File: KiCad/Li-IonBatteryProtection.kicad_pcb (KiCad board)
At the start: 2 copper layers, 1 part, among them Q1 IRF540N

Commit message: Net wiring on PCB is done.
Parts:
- added C1: 0.1uf, Capacitors_ThroughHole:C_Rect_L4_W2.5_P2.5, F.Cu at (184.2, 119.4)
- added C2: 0.22uf, Capacitors_ThroughHole:C_Rect_L7_W2_P5, F.Cu at (190.5, 116.8)
- added C3: 0.001uf, Capacitors_ThroughHole:C_Rect_L7_W2_P5, F.Cu at (188.0, 101.6)
- added C4: 47uf, Capacitors_ThroughHole:C_Radial_D5_L11_P2.5, F.Cu at (203.2, 105.4)
- added D1: 1N4728, Diodes_ThroughHole:Diode_DO-41_SOD81_Horizontal_RM10, F.Cu at (67.3, 113.0)
- added D2: 1N4728, Diodes_ThroughHole:Diode_DO-41_SOD81_Horizontal_RM10, F.Cu at (99.1, 113.0)
- added D3: 1N4728, Diodes_ThroughHole:Diode_DO-41_SOD81_Horizontal_RM10, F.Cu at (130.8, 113.0)
- added D4: 1N4728, Diodes_ThroughHole:Diode_DO-41_SOD81_Horizontal_RM10, F.Cu at (162.6, 113.0)
- added J1: CONN_02X03, Pin_Headers:Pin_Header_Straight_2x03, F.Cu at (218.4, 82.5)
- added J2: CONN_01X02, Terminal_Blocks:TerminalBlock_Pheonix_MKDS1.5-2pol, F.Cu at (209.6, 82.5)
- added Q2: 2N2222A, TO_SOT_Packages_THT:TO-18_3Pin, F.Cu at (201.9, 119.4)
- added Q3: 2N2222A, TO_SOT_Packages_THT:TO-18_3Pin, F.Cu at (81.3, 90.2)
- added Q4: 2N2222A, TO_SOT_Packages_THT:TO-18_3Pin, F.Cu at (113.0, 90.2)
- added Q5: 2N2222A, TO_SOT_Packages_THT:TO-18_3Pin, F.Cu at (144.8, 90.2)
- added Q6: 2N2222A, TO_SOT_Packages_THT:TO-18_3Pin, F.Cu at (176.5, 90.2)
- added R1: 10k, Resistors_ThroughHole:Resistor_Horizontal_RM10mm, F.Cu at (67.3, 105.4)
- added R10: 1Meg, Potentiometers:Potentiometer_Bourns_3296Y_3-8Zoll_Angular_ScrewUp, F.Cu at (96.5, 119.4)
- added R11: 47k, Resistors_ThroughHole:Resistor_Horizontal_RM10mm, F.Cu at (105.4, 92.7)
- added R12: 100k, Resistors_ThroughHole:Resistor_Horizontal_RM10mm, F.Cu at (88.9, 90.2)
- added R13: 100, Resistors_ThroughHole:Resistor_Horizontal_RM10mm, F.Cu at (113.0, 96.5)
- added R14: 120, Resistors_ThroughHole:Resistor_Horizontal_RM10mm, F.Cu at (88.9, 82.5)
- added R15: 10k, Resistors_ThroughHole:Resistor_Horizontal_RM10mm, F.Cu at (130.8, 105.4)
- added R16: 1k, Resistors_ThroughHole:Resistor_Horizontal_RM7mm, F.Cu at (120.7, 97.8)
- added R17: 1Meg, Potentiometers:Potentiometer_Bourns_3296Y_3-8Zoll_Angular_ScrewUp, F.Cu at (128.3, 119.4)
- added R18: 47k, Resistors_ThroughHole:Resistor_Horizontal_RM10mm, F.Cu at (137.2, 92.7)
- added R19: 100k, Resistors_ThroughHole:Resistor_Horizontal_RM10mm, F.Cu at (120.7, 90.2)
- added R2: 1k, Resistors_ThroughHole:Resistor_Horizontal_RM7mm, F.Cu at (57.1, 97.8)
- added R20: 100, Resistors_ThroughHole:Resistor_Horizontal_RM10mm, F.Cu at (144.8, 96.5)
- added R21: 120, Resistors_ThroughHole:Resistor_Horizontal_RM10mm, F.Cu at (120.7, 82.5)
- added R22: 10k, Resistors_ThroughHole:Resistor_Horizontal_RM10mm, F.Cu at (162.6, 105.4)
- added R23: 1k, Resistors_ThroughHole:Resistor_Horizontal_RM7mm, F.Cu at (152.4, 97.8)
- added R24: 1Meg, Potentiometers:Potentiometer_Bourns_3296Y_3-8Zoll_Angular_ScrewUp, F.Cu at (160.0, 119.4)
- added R25: 47k, Resistors_ThroughHole:Resistor_Horizontal_RM10mm, F.Cu at (168.9, 92.7)
- added R26: 100k, Resistors_ThroughHole:Resistor_Horizontal_RM10mm, F.Cu at (152.4, 90.2)
- added R27: 100, Resistors_ThroughHole:Resistor_Horizontal_RM10mm, F.Cu at (176.5, 96.5)
- added R28: 120, Resistors_ThroughHole:Resistor_Horizontal_RM10mm, F.Cu at (152.4, 82.5)
- added R29: 5.1k, Resistors_ThroughHole:Resistor_Horizontal_RM10mm, F.Cu at (194.3, 110.5)
- added R3: 1Meg, Potentiometers:Potentiometer_Bourns_3296Y_3-8Zoll_Angular_ScrewUp, F.Cu at (64.8, 119.4)
- added R30: 3.3k, Resistors_ThroughHole:Resistor_Horizontal_RM10mm, F.Cu at (196.8, 88.9)
- added R31: 20k, Resistors_ThroughHole:Resistor_Horizontal_RM10mm, F.Cu at (194.3, 80.0)
- added R4: 47k, Resistors_ThroughHole:Resistor_Horizontal_RM10mm, F.Cu at (73.7, 94.0)
- added R5: 100k, Resistors_ThroughHole:Resistor_Horizontal_RM10mm, F.Cu at (57.1, 90.2)
- added R6: 100, Resistors_ThroughHole:Resistor_Horizontal_RM10mm, F.Cu at (81.3, 96.5)
- added R7: 120, Resistors_ThroughHole:Resistor_Horizontal_RM10mm, F.Cu at (57.1, 82.5)
- added R8: 10k, Resistors_ThroughHole:Resistor_Horizontal_RM10mm, F.Cu at (99.1, 105.4)
- added R9: 1k, Resistors_ThroughHole:Resistor_Horizontal_RM7mm, F.Cu at (88.9, 97.8)
- added U1: LM311N, Housings_DIP:DIP-8_W7.62mm, F.Cu at (74.9, 113.0)
- added U2: PC817, Housings_DIP:DIP-4_W7.62mm, F.Cu at (74.9, 80.0)
- added U3: LM311N, Housings_DIP:DIP-8_W7.62mm, F.Cu at (106.7, 113.0)
- added U4: PC817, Housings_DIP:DIP-4_W7.62mm, F.Cu at (106.7, 80.0)
- added U5: LM311N, Housings_DIP:DIP-8_W7.62mm, F.Cu at (138.4, 113.0)
- added U6: PC817, Housings_DIP:DIP-4_W7.62mm, F.Cu at (138.4, 80.0)
- added U7: LM311N, Housings_DIP:DIP-8_W7.62mm, F.Cu at (170.2, 113.0)
- added U8: PC817, Housings_DIP:DIP-4_W7.62mm, F.Cu at (170.2, 80.0)
- moved Q1 80.7 mm to (219.7, 118.1)
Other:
- board outline added: 176.5 x 54.6 mm

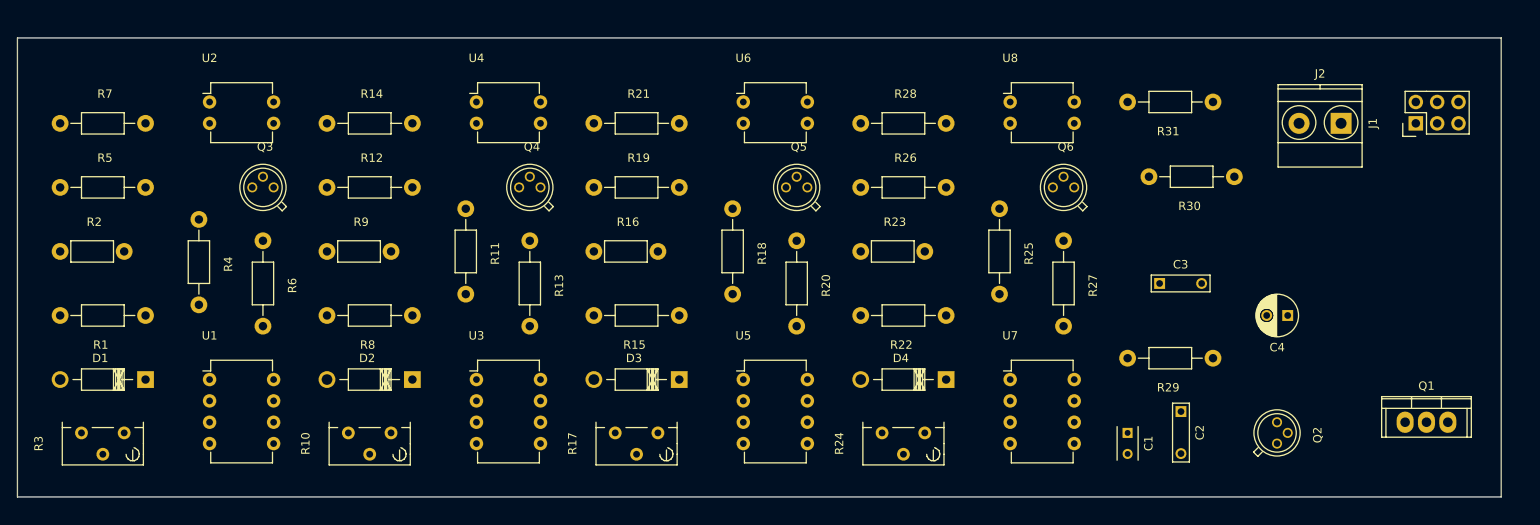
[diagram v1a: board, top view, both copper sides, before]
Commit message: Updated the PDB layout.
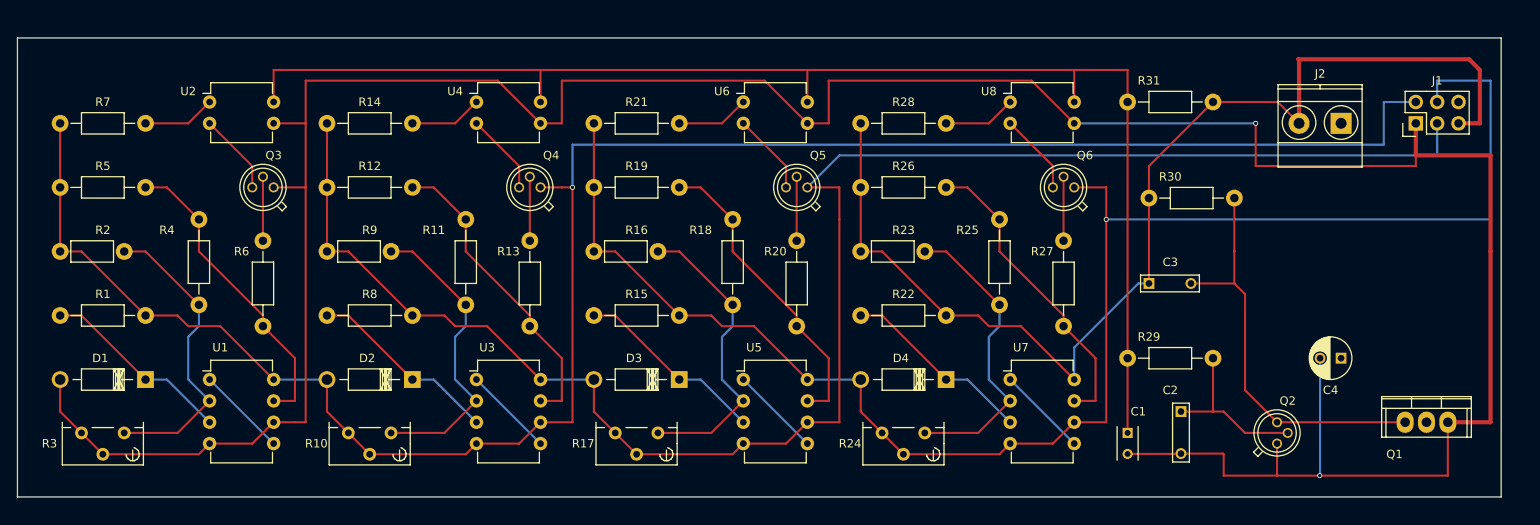
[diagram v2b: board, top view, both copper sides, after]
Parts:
- moved C4 8.13 mm to (209.6, 110.5)
- moved R30 2.54 mm to (196.8, 91.4)
- moved C3 1.27 mm to (186.7, 101.6)
- moved R11 1.27 mm to (105.4, 94.0)
- moved R18 1.27 mm to (137.2, 94.0)
- moved R25 1.27 mm to (168.9, 94.0)
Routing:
- net Battery-GND: track 0.00 -> 354.2 mm, vias 0 -> 2
- net Battery-1: track 0.00 -> 232.2 mm, vias 0 -> 1
- net Battery-2: track 0.00 -> 202.1 mm
- net Battery-3: track 0.00 -> 192.9 mm, vias 0 -> 1
- net Net-(C1-Pad1): track 0.00 -> 160.0 mm
- net Battery-4: track 0.00 -> 137.5 mm
- net Net-(C3-Pad2): track 0.00 -> 49.3 mm
- net Net-(R4-Pad1): track 0.00 -> 36.8 mm
- net Net-(R11-Pad1): track 0.00 -> 36.8 mm
- net Net-(R25-Pad1): track 0.00 -> 36.8 mm
- net Net-(R18-Pad1): track 0.00 -> 36.8 mm
- net Net-(R2-Pad2): track 0.00 -> 36.3 mm
- net Net-(R10-Pad1): track 0.00 -> 36.3 mm
- net Net-(R23-Pad2): track 0.00 -> 36.3 mm
- net Net-(R16-Pad2): track 0.00 -> 36.3 mm
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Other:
- net class Power added: clearance 0.4, trace_width 0.5, via_dia 1.2, via_drill 0.8

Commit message: Updated the TO-220 footprint. Started fill zones.
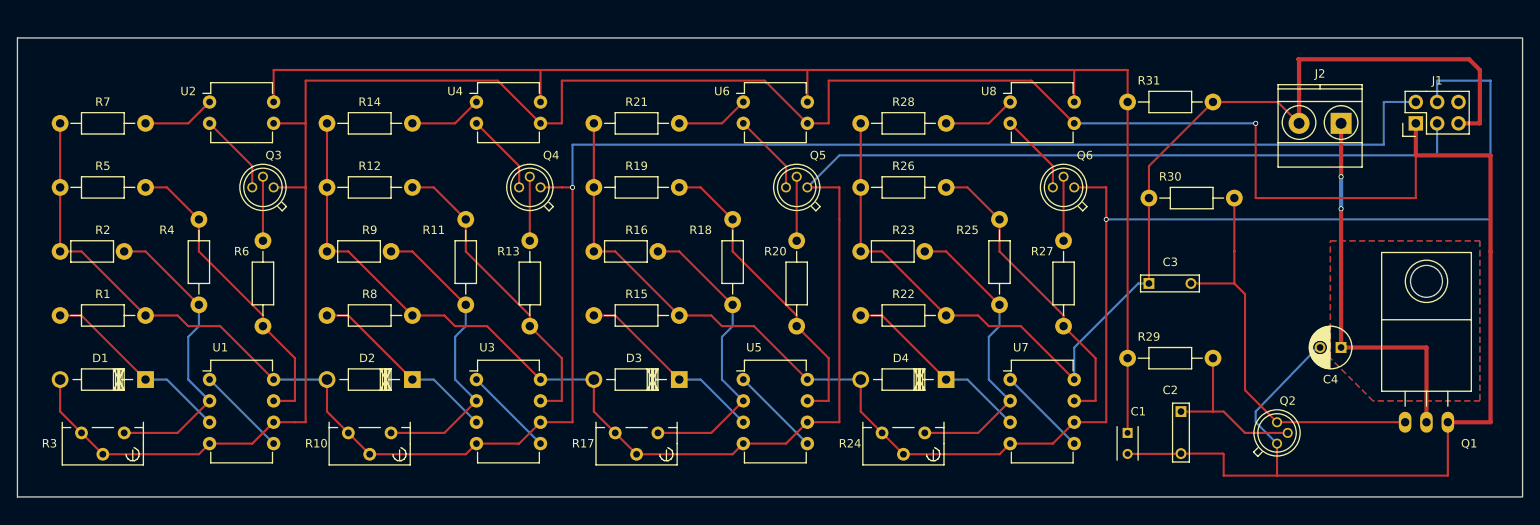
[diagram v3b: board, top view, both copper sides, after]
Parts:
- Q1: footprint TO-220 -> TO_SOT_Packages_THT:TO-220_Neutral123_Horizontal
- moved C4 1.27 mm to (209.6, 109.2)
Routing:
- net Net-(C4-Pad1): track 0.00 -> 45.7 mm, vias 0 -> 2
- net Battery-GND: track 354.2 -> 363.6 mm, vias 2 -> 1
- added copper zone on B.Cu, net Battery-4
- added copper zone on F.Cu, net Battery-4
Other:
- board size 176.5 x 54.6 mm -> 179.1 x 54.6 mm
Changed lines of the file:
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@@
   (general
     (links 118)
-    (no_connects 3)
-    (area 51.994999 72.314999 228.675001 127.075001)
+    (no_connects 0)
+    (area 51.994999 72.314999 231.215001 127.075001)
     (thickness 1.6)
     (drawings 4)
-    (tracks 283)
+    (tracks 291)
     (zones 0)
     (modules 55)
@@
   )
   (setup
-    (last_trace_width 0.25)
+    (last_trace_width 0.5)
     (user_trace_width 0.5)
     (trace_clearance 0.25)
     (zone_clearance 0.508)
-    (zone_45_only no)
+    (zone_45_only yes)
     (trace_min 0.25)
     (segment_width 0.2)
@@
     (uvia_drill 0.2)
   )
-  (module TO-220 (layer F.Cu)
-    (at 219.71 118.11)
-    (descr "Non Isolated JEDEC TO-220 Package")
-    (tags "Power Integration YN Package")
-    (fp_text reference Q1 (at -3.81 3.81) (layer F.SilkS)
-      (effects (font (size 1 1) (thickness 0.15)))
-    )
-    (fp_text value IRF540N (at 2.54 3.81) (layer F.Fab)
-      (effects (font (size 1 1) (thickness 0.15)))
-    )
-    (fp_line (start 4.826 -1.651) (end 4.826 1.778) (layer F.SilkS) (width 0.15))
-    (fp_line (start -4.826 -1.651) (end -4.826 1.778) (layer F.SilkS) (width 0.15))
-    (fp_line (start 5.334 -2.794) (end -5.334 -2.794) (layer F.SilkS) (width 0.15))
-    (fp_line (start 1.778 -1.778) (end 1.778 -3.048) (layer F.SilkS) (width 0.15))
-    (fp_line (start -1.778 -1.778) (end -1.778 -3.048) (layer F.SilkS) (width 0.15))
-    (fp_line (start -5.334 -1.651) (end 5.334 -1.651) (layer F.SilkS) (width 0.15))
-    (fp_line (start 5.334 1.778) (end -5.334 1.778) (layer F.SilkS) (width 0.15))
-    (fp_line (start -5.334 -3.048) (end -5.334 1.778) (layer F.SilkS) (width 0.15))
-    (fp_line (start 5.334 -3.048) (end 5.334 1.778) (layer F.SilkS) (width 0.15))
-    (fp_line (start 5.334 -3.048) (end -5.334 -3.048) (layer F.SilkS) (width 0.15))
-    (pad 2 thru_hole oval (at 0 0) (size 2.032 2.54) (drill 1.143) (layers *.Cu *.Mask F.SilkS)
-      (net 1 "Net-(C4-Pad1)"))
-    (pad 3 thru_hole oval (at 2.54 0) (size 2.032 2.54) (drill 1.143) (layers *.Cu *.Mask F.SilkS)
-      (net 2 Battery-GND))
-    (pad 1 thru_hole oval (at -2.54 0) (size 2.032 2.54) (drill 1.143) (layers *.Cu *.Mask F.SilkS)
-      (net 3 "Net-(C3-Pad2)"))
-  )
   (module Capacitors_ThroughHole:C_Rect_L4_W2.5_P2.5 (layer F.Cu)
     (at 184.15 119.38 270)
@@
   )
   (module Capacitors_ThroughHole:C_Radial_D5_L11_P2.5 (layer F.Cu)
-    (at 209.55 110.49 180)
+    (at 209.55 109.22 180)
     (descr "Radial Electrolytic Capacitor Diameter 5mm x Length 11mm, Pitch 2.5mm")
     (tags "Electrolytic Capacitor")
@@
     )
   )
+  (module TO_SOT_Packages_THT:TO-220_Neutral123_Horizontal (layer F.Cu)
+    (at 219.71 118.11)
+    (descr "TO-220, Neutral, Horizontal,")
+    (tags "TO-220, Neutral, Horizontal,")
+    (fp_text reference Q1 (at 5.08 2.54) (layer F.SilkS)
+      (effects (font (size 1 1) (thickness 0.15)))
+    )
+    (fp_text value IRF540N (at -0.29972 3.44932) (layer F.Fab)
+      (effects (font (size 1 1) (thickness 0.15)))
+    )
+    (fp_circle (center 0 -16.764) (end 1.778 -14.986) (layer F.SilkS) (width 0.15))
+    (fp_line (start -2.54 -3.683) (end -2.54 -1.905) (layer F.SilkS) (width 0.15))
+    (fp_line (start 0 -3.683) (end 0 -1.905) (layer F.SilkS) (width 0.15))
+    (fp_line (start 2.54 -3.683) (end 2.54 -1.905) (layer F.SilkS) (width 0.15))
+    (fp_line (start 5.334 -12.192) (end 5.334 -20.193) (layer F.SilkS) (width 0.15))
+    (fp_line (start 5.334 -20.193) (end -5.334 -20.193) (layer F.SilkS) (width 0.15))
+    (fp_line (start -5.334 -20.193) (end -5.334 -12.192) (layer F.SilkS) (width 0.15))
+    (fp_line (start 5.334 -3.683) (end 5.334 -12.192) (layer F.SilkS) (width 0.15))
+    (fp_line (start 5.334 -12.192) (end -5.334 -12.192) (layer F.SilkS) (width 0.15))
+    (fp_line (start -5.334 -12.192) (end -5.334 -3.683) (layer F.SilkS) (width 0.15))
+    (fp_line (start 0 -3.683) (end -5.334 -3.683) (layer F.SilkS) (width 0.15))
+    (fp_line (start 0 -3.683) (end 5.334 -3.683) (layer F.SilkS) (width 0.15))
+    (pad 2 thru_hole oval (at 0 0 90) (size 2.49936 1.50114) (drill 1.00076) (layers *.Cu *.Mask F.SilkS)
+      (net 1 "Net-(C4-Pad1)"))
+    (pad 1 thru_hole oval (at -2.54 0 90) (size 2.49936 1.50114) (drill 1.00076) (layers *.Cu *.Mask F.SilkS)
+      (net 3 "Net-(C3-Pad2)"))
+    (pad 3 thru_hole oval (at 2.54 0 90) (size 2.49936 1.50114) (drill 1.00076) (layers *.Cu *.Mask F.SilkS)
+      (net 2 Battery-GND))
+    (pad "" np_thru_hole circle (at 0 -16.764 90) (size 3.79984 3.79984) (drill 3.79984) (layers *.Cu *.Mask F.SilkS))
+    (model TO_SOT_Packages_THT.3dshapes/TO-220_Neutral123_Horizontal.wrl
+      (at (xyz 0 0 0))
+      (scale (xyz 0.3937 0.3937 0.3937))
+      (rotate (xyz 0 0 0))
+    )
+  )
   (gr_line (start 52.07 127) (end 52.07 72.39) (angle 90) (layer Edge.Cuts) (width 0.15))
-  (gr_line (start 228.6 127) (end 52.07 127) (angle 90) (layer Edge.Cuts) (width 0.15))
-  (gr_line (start 228.6 72.39) (end 228.6 127) (angle 90) (layer Edge.Cuts) (width 0.15))
-  (gr_line (start 52.07 72.39) (end 228.6 72.39) (angle 90) (layer Edge.Cuts) (width 0.15))
-  (segment (start 218.44 86.36) (end 218.44 87.63) (width 0.25) (layer F.Cu) (net 2))
-  (segment (start 218.44 87.63) (end 199.39 87.63) (width 0.25) (layer F.Cu) (net 2))
+  (gr_line (start 231 127) (end 52.07 127) (angle 90) (layer Edge.Cuts) (width 0.15))
+  (gr_line (start 231.14 72.39) (end 231.14 127) (angle 90) (layer Edge.Cuts) (width 0.15))
+  (gr_line (start 52.07 72.39) (end 231 72.39) (angle 90) (layer Edge.Cuts) (width 0.15))
+  (segment (start 209.55 109.22) (end 219.71 109.22) (width 0.5) (layer F.Cu) (net 1) (status 10))
+  (segment (start 219.71 109.22) (end 219.71 118.11) (width 0.5) (layer F.Cu) (net 1))
+  (segment (start 209.55 82.55) (end 209.55 88.9) (width 0.5) (layer F.Cu) (net 1))
+  (segment (start 209.55 92.71) (end 209.55 109.22) (width 0.5) (layer F.Cu) (net 1) (status 20))
+  (via (at 209.55 92.71) (size 0.6) (drill 0.4) (layers F.Cu B.Cu) (net 1))
+  (segment (start 209.55 88.9) (end 209.55 92.71) (width 0.5) (layer B.Cu) (net 1))
+  (via (at 209.55 88.9) (size 0.6) (drill 0.4) (layers F.Cu B.Cu) (net 1))
+  (segment (start 207.05 109.22) (end 206.502 109.474) (width 0.25) (layer B.Cu) (net 2) (status 80030))
+  (segment (start 206.502 109.474) (end 199.39 116.84) (width 0.25) (layer B.Cu) (net 2) (status 80010))
+  (segment (start 199.39 116.84) (end 199.39 118.11) (width 0.25) (layer B.Cu) (net 2) (status 80000))
+  (segment (start 199.39 118.11) (end 201.93 120.65) (width 0.25) (layer B.Cu) (net 2) (status 80000))
+  (segment (start 218.44 86.36) (end 218.44 91.44) (width 0.25) (layer F.Cu) (net 2))
+  (segment (start 218.44 91.44) (end 199.39 91.44) (width 0.25) (layer F.Cu) (net 2))
   (via (at 199.39 82.55) (size 0.6) (drill 0.4) (layers F.Cu B.Cu) (net 2))
-  (segment (start 199.39 87.63) (end 199.39 82.55) (width 0.25) (layer F.Cu) (net 2))
+  (segment (start 199.39 91.44) (end 199.39 82.55) (width 0.25) (layer F.Cu) (net 2))
   (segment (start 177.8 82.55) (end 199.39 82.55) (width 0.25) (layer B.Cu) (net 2))
   (segment (start 201.93 120.65) (end 201.93 124.46) (width 0.25) (layer F.Cu) (net 2) (status 10))
-  (segment (start 207.05 110.49) (end 207.05 124.42) (width 0.25) (layer B.Cu) (net 2) (status 10))
-  (via (at 207.01 124.46) (size 0.6) (drill 0.4) (layers F.Cu B.Cu) (net 2))
-  (segment (start 207.05 124.42) (end 207.01 124.46) (width 0.25) (layer B.Cu) (net 2))
   (segment (start 86.36 82.55) (end 86.36 77.47) (width 0.25) (layer F.Cu) (net 2))
   (segment (start 109.22 77.47) (end 114.3 82.55) (width 0.25) (layer F.Cu) (net 2))
@@
   (segment (start 138.43 113.03) (end 146.05 120.65) (width 0.25) (layer B.Cu) (net 37))
   (segment (start 170.18 113.03) (end 177.8 120.65) (width 0.25) (layer B.Cu) (net 38))
+  (zone (net 6) (net_name Battery-4) (layer F.Cu) (hatch edge 0.508)
+    (connect_pads (clearance 0.508))
+    (min_thickness 0.254)
+    (fill yes (arc_segments 16) (thermal_gap 0.508) (thermal_bridge_width 0.508))
+    (polygon
+      (pts
+        (xy 226.06 115.57) (xy 213.36 115.57) (xy 208.28 110.49) (xy 208.28 96.52) (xy 226.06 96.52)
+        (xy 226.06 115.57)
+      )
+    )
+  )
+  (zone (net 6) (net_name Battery-4) (layer B.Cu) (hatch edge 0.508)
+    (connect_pads (clearance 0.508))
+    (min_thickness 0.254)
+    (fill yes (arc_segments 16) (thermal_gap 0.508) (thermal_bridge_width 0.508))
+    (polygon
+      (pts
+        (xy 226.06 115.57) (xy 213.36 115.57) (xy 208.28 110.49) (xy 208.28 96.52) (xy 226.06 96.52)
+        (xy 226.06 115.57)
+      )
+    )
+  )
 )
